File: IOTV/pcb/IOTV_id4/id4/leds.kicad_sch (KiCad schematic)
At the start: 50 parts, among them Q1 S8050, Q10 S8050, Q11 S8050, Q12 S8050, Q2 S8050, Q3 S8050, Q7 S8050, Q8 S8050, Q9 S8050

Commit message: PCB - ID4
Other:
- note added: "LED 5"
- note removed: "LED 0"

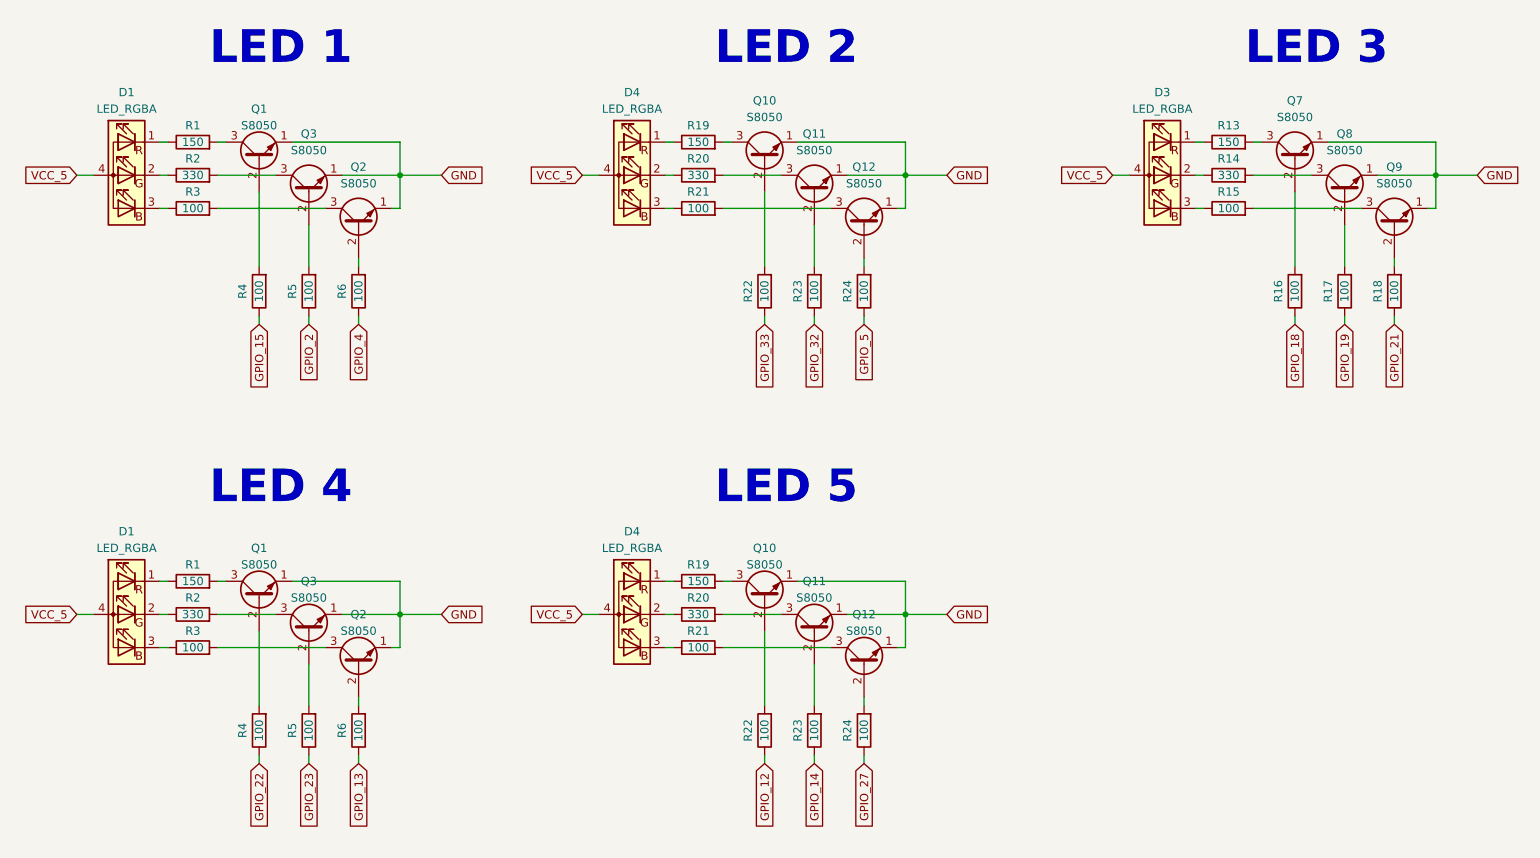
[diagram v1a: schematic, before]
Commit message: pcb id4 - rezonit OK
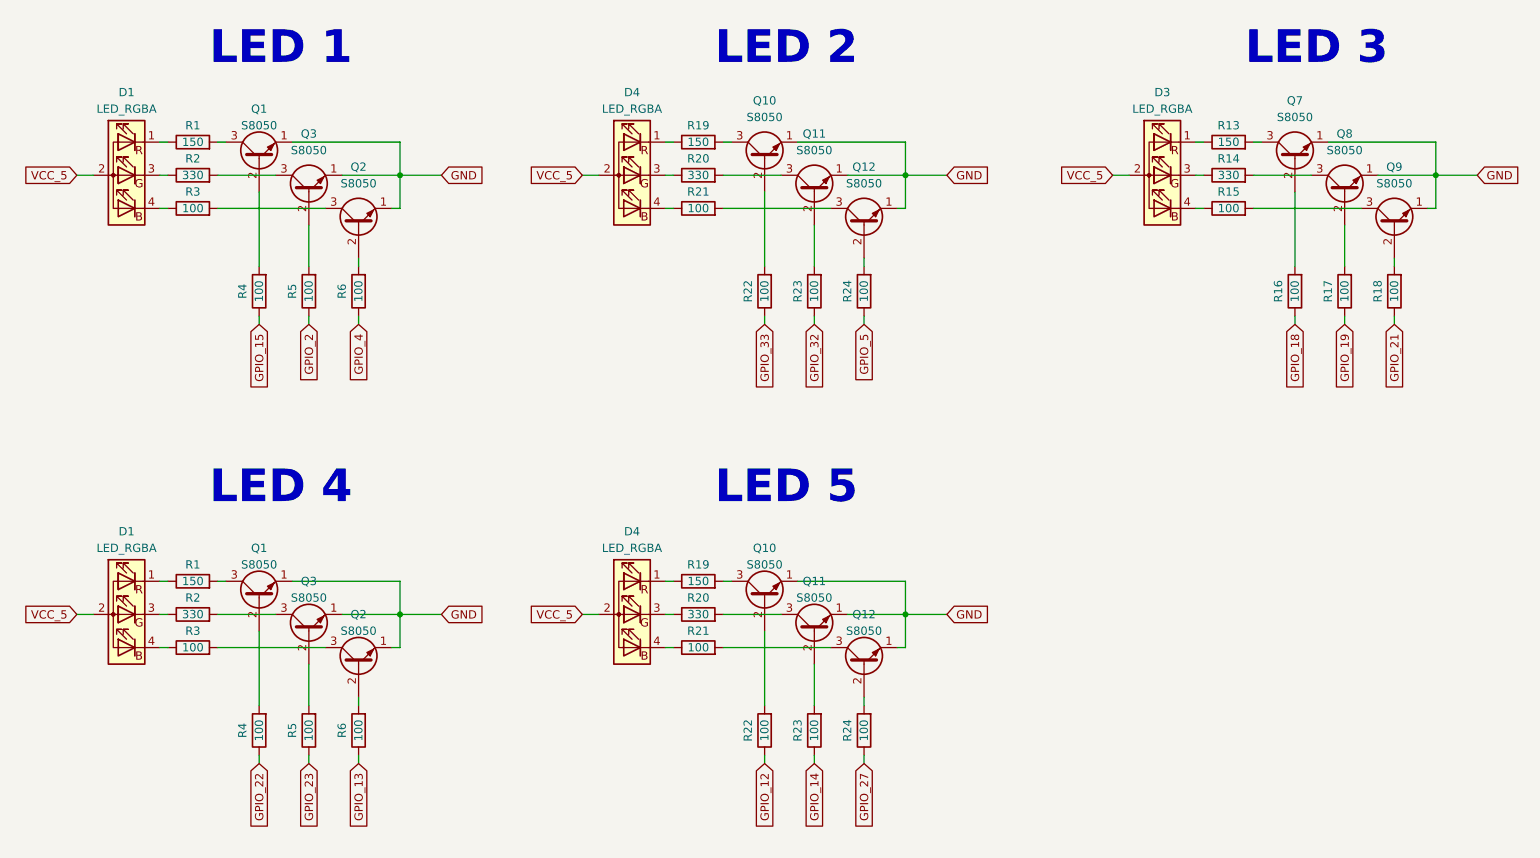
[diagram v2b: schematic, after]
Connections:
- net VCC_5: now also D1.2 (A), D1.2 (A), D3.2 (A), D4.2 (A), D4.2 (A); no longer D1.4 (A), D1.4 (A), D3.4 (A), D4.4 (A), D4.4 (A)
- net at R21.1: now also D4.4 (BK); no longer D4.3 (BK) (x2)
- net at R2.1: now also D1.3 (GK); no longer D1.2 (GK) (x2)
- net at R3.1: now also D1.4 (BK); no longer D1.3 (BK) (x2)
- net at R15.1: now also D3.4 (BK); no longer D3.3 (BK)
- net at R20.1: now also D4.3 (GK); no longer D4.2 (GK) (x2)
- net at R14.1: now also D3.3 (GK); no longer D3.2 (GK)
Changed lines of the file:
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@@
     )
   )
-  (symbol (lib_id "Device:LED_RGBA") (at 48.26 128.27 0) (mirror y) (unit 1)
+  (symbol (lib_name "LED_RGBA_4") (lib_id "Device:LED_RGBA") (at 48.26 128.27 0) (mirror y) (unit 1)
     (in_bom yes) (on_board yes) (dnp no)
     (property "Reference" "D1" (at 48.26 115.57 0)
@@
     )
     (pin "1")
-    (pin "2")
     (pin "3")
     (pin "4")
+    (pin "2")
     (instances
       (project "id4"
@@
     )
   )
-  (symbol (lib_id "Device:LED_RGBA") (at 125.73 60.96 0) (mirror y) (unit 1)
+  (symbol (lib_name "LED_RGBA_2") (lib_id "Device:LED_RGBA") (at 125.73 60.96 0) (mirror y) (unit 1)
     (in_bom yes) (on_board yes) (dnp no)
     (property "Reference" "D4" (at 125.73 48.26 0)
@@
     )
   )
-  (symbol (lib_id "Device:LED_RGBA") (at 48.26 60.96 0) (mirror y) (unit 1)
+  (symbol (lib_name "LED_RGBA_1") (lib_id "Device:LED_RGBA") (at 48.26 60.96 0) (mirror y) (unit 1)
     (in_bom yes) (on_board yes) (dnp no)
     (property "Reference" "D1" (at 48.26 48.26 0)
@@
     )
   )
-  (symbol (lib_id "Device:LED_RGBA") (at 207.01 60.96 0) (mirror y) (unit 1)
+  (symbol (lib_name "LED_RGBA_3") (lib_id "Device:LED_RGBA") (at 207.01 60.96 0) (mirror y) (unit 1)
     (in_bom yes) (on_board yes) (dnp no)
     (property "Reference" "D3" (at 207.01 48.26 0)

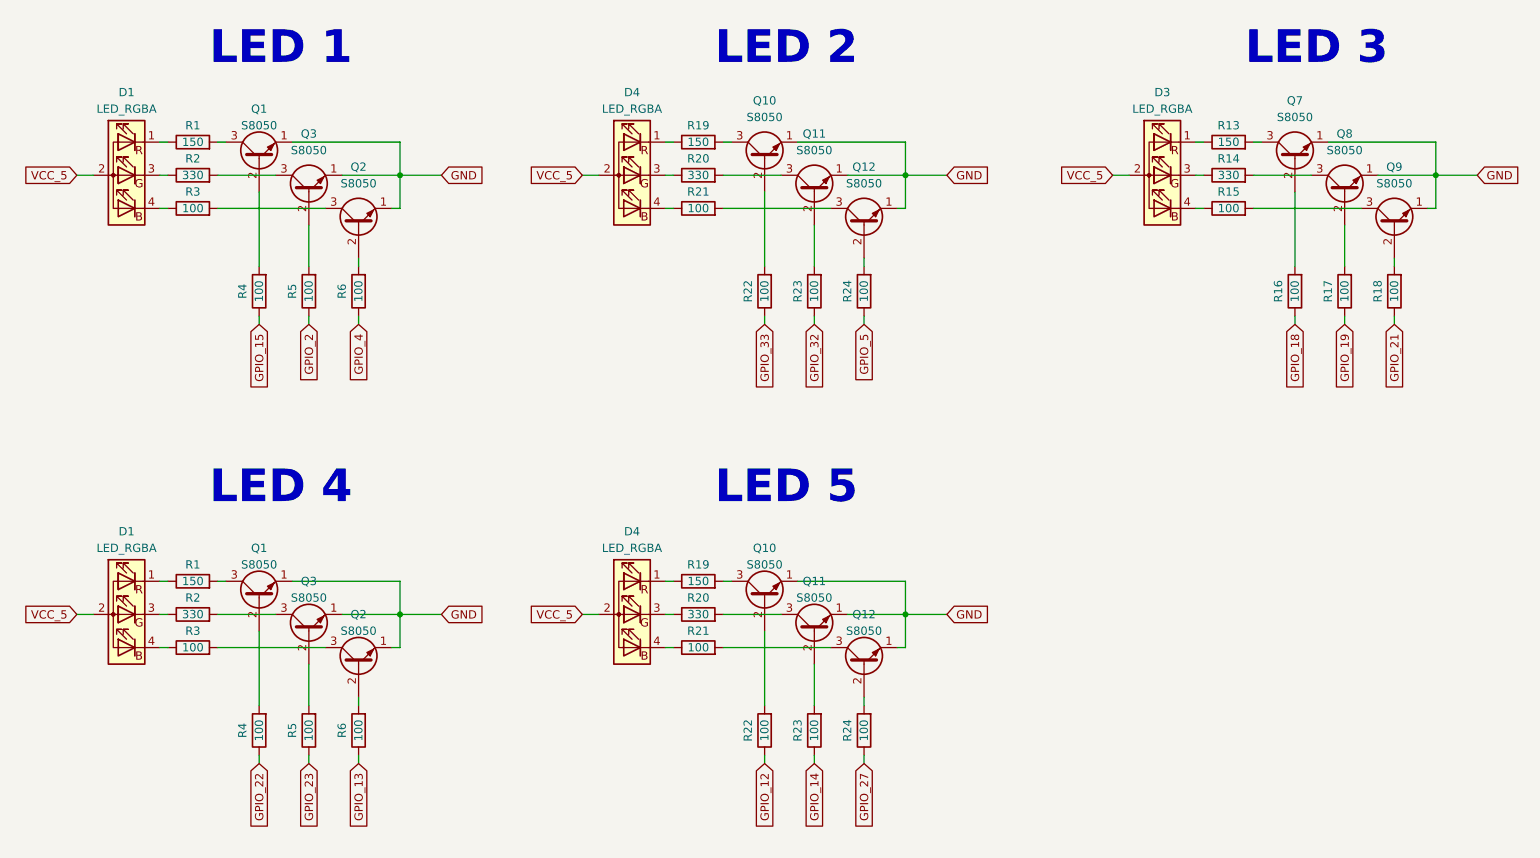
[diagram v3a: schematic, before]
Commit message: PCB id4 кнопки на землю
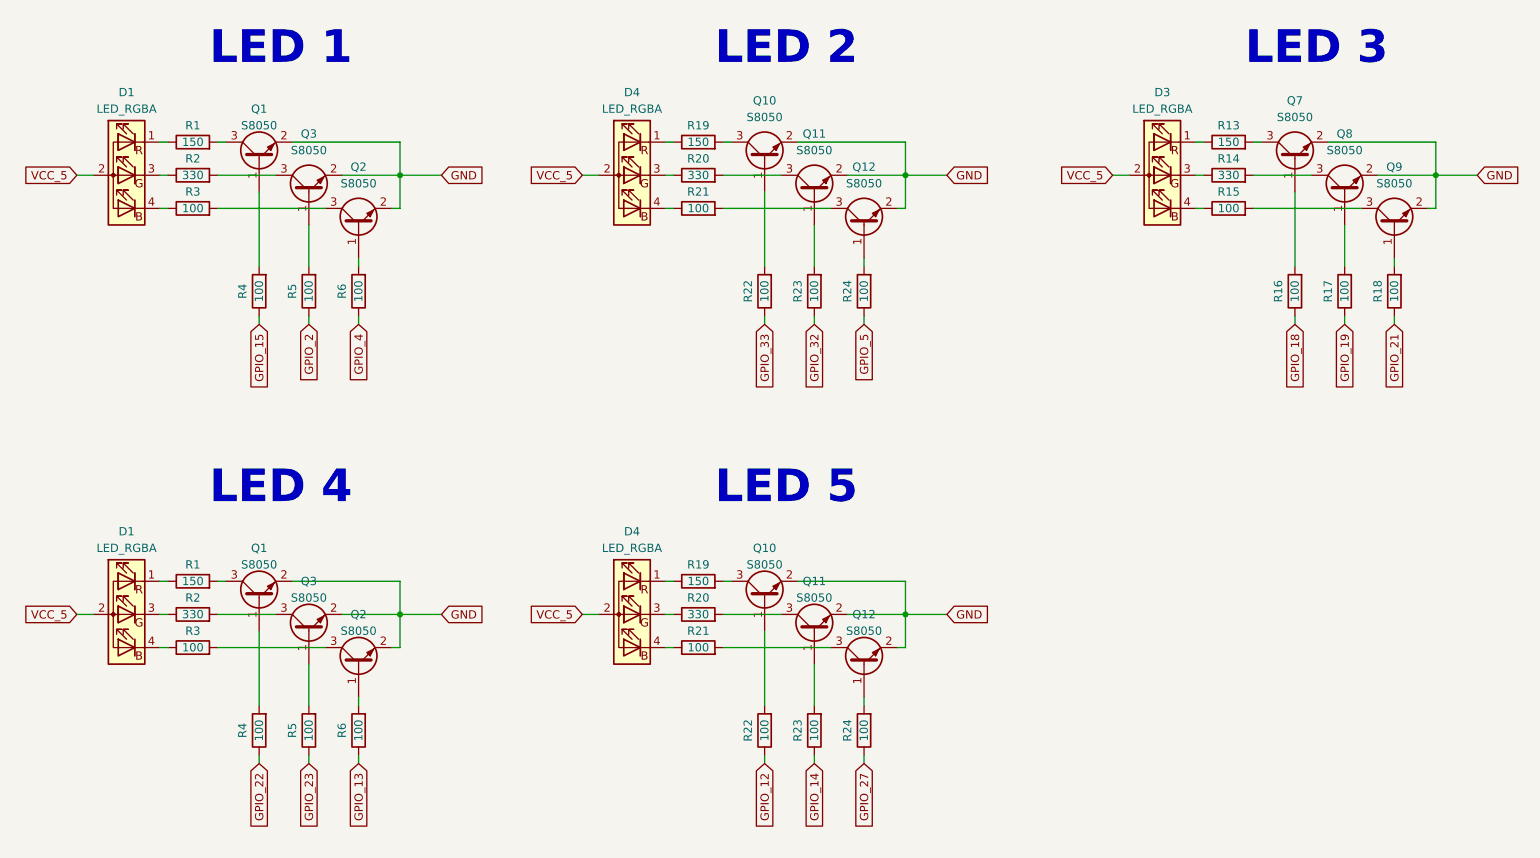
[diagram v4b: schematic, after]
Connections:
- net GND: now also Q1.2 (E), Q1.2 (E), Q10.2 (E), Q10.2 (E), Q11.2 (E), Q11.2 (E), Q12.2 (E), Q12.2 (E), Q2.2 (E), Q2.2 (E), Q3.2 (E), Q3.2 (E), Q7.2 (E), Q8.2 (E), Q9.2 (E); no longer Q1.1 (E), Q1.1 (E), Q10.1 (E), Q10.1 (E), Q11.1 (E), Q11.1 (E), Q12.1 (E), Q12.1 (E), Q2.1 (E), Q2.1 (E), Q3.1 (E), Q3.1 (E), Q7.1 (E), Q8.1 (E), Q9.1 (E)
- net at R16.2: now also Q7.1 (B); no longer Q7.2 (B)
- net at R24.2: now also Q12.1 (B); no longer Q12.2 (B) (x2)
- net at R6.2: now also Q2.1 (B); no longer Q2.2 (B) (x2)
- net at R5.2: now also Q3.1 (B); no longer Q3.2 (B) (x2)
- net at R4.2: now also Q1.1 (B); no longer Q1.2 (B) (x2)
- net at R22.2: now also Q10.1 (B); no longer Q10.2 (B) (x2)
- net at R23.2: now also Q11.1 (B); no longer Q11.2 (B) (x2)
- net at R17.2: now also Q8.1 (B); no longer Q8.2 (B)
- net at R18.2: now also Q9.1 (B); no longer Q9.2 (B)
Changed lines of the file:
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@@
     )
   )
-  (symbol (lib_id "Transistor_BJT:S8050") (at 227.33 58.42 90) (unit 1)
+  (symbol (lib_name "S8050_7") (lib_id "Transistor_BJT:S8050") (at 227.33 58.42 90) (unit 1)
     (in_bom yes) (on_board yes) (dnp no) (fields_autoplaced)
     (property "Reference" "Q7" (at 227.33 49.53 90)
@@
     )
   )
-  (symbol (lib_id "Transistor_BJT:S8050") (at 68.58 125.73 90) (unit 1)
+  (symbol (lib_name "S8050_10") (lib_id "Transistor_BJT:S8050") (at 68.58 125.73 90) (unit 1)
     (in_bom yes) (on_board yes) (dnp no) (fields_autoplaced)
     (property "Reference" "Q1" (at 68.58 118.11 90)
@@
     )
   )
-  (symbol (lib_id "Transistor_BJT:S8050") (at 76.2 130.81 90) (unit 1)
+  (symbol (lib_name "S8050_11") (lib_id "Transistor_BJT:S8050") (at 76.2 130.81 90) (unit 1)
     (in_bom yes) (on_board yes) (dnp no) (fields_autoplaced)
     (property "Reference" "Q3" (at 76.2 123.19 90)
@@
     )
   )
-  (symbol (lib_id "Transistor_BJT:S8050") (at 68.58 58.42 90) (unit 1)
+  (symbol (lib_name "S8050_1") (lib_id "Transistor_BJT:S8050") (at 68.58 58.42 90) (unit 1)
     (in_bom yes) (on_board yes) (dnp no) (fields_autoplaced)
     (property "Reference" "Q1" (at 68.58 50.8 90)
@@
     )
   )
-  (symbol (lib_id "Transistor_BJT:S8050") (at 146.05 58.42 90) (unit 1)
+  (symbol (lib_name "S8050_4") (lib_id "Transistor_BJT:S8050") (at 146.05 58.42 90) (unit 1)
     (in_bom yes) (on_board yes) (dnp no) (fields_autoplaced)
     (property "Reference" "Q10" (at 146.05 49.53 90)
@@
     )
   )
-  (symbol (lib_id "Transistor_BJT:S8050") (at 83.82 68.58 90) (unit 1)
+  (symbol (lib_name "S8050_3") (lib_id "Transistor_BJT:S8050") (at 83.82 68.58 90) (unit 1)
     (in_bom yes) (on_board yes) (dnp no) (fields_autoplaced)
     (property "Reference" "Q2" (at 83.82 59.69 90)
@@
     )
   )
-  (symbol (lib_id "Transistor_BJT:S8050") (at 146.05 125.73 90) (unit 1)
+  (symbol (lib_name "S8050_13") (lib_id "Transistor_BJT:S8050") (at 146.05 125.73 90) (unit 1)
     (in_bom yes) (on_board yes) (dnp no) (fields_autoplaced)
     (property "Reference" "Q10" (at 146.05 118.11 90)
@@
     )
   )
-  (symbol (lib_id "Transistor_BJT:S8050") (at 153.67 130.81 90) (unit 1)
+  (symbol (lib_name "S8050_14") (lib_id "Transistor_BJT:S8050") (at 153.67 130.81 90) (unit 1)
     (in_bom yes) (on_board yes) (dnp no) (fields_autoplaced)
     (property "Reference" "Q11" (at 153.67 123.19 90)
@@
     )
   )
-  (symbol (lib_id "Transistor_BJT:S8050") (at 76.2 63.5 90) (unit 1)
+  (symbol (lib_name "S8050_2") (lib_id "Transistor_BJT:S8050") (at 76.2 63.5 90) (unit 1)
     (in_bom yes) (on_board yes) (dnp no) (fields_autoplaced)
     (property "Reference" "Q3" (at 76.2 54.61 90)
@@
     )
   )
-  (symbol (lib_id "Transistor_BJT:S8050") (at 242.57 68.58 90) (unit 1)
+  (symbol (lib_name "S8050_9") (lib_id "Transistor_BJT:S8050") (at 242.57 68.58 90) (unit 1)
     (in_bom yes) (on_board yes) (dnp no) (fields_autoplaced)
     (property "Reference" "Q9" (at 242.57 59.69 90)
@@
     )
   )
-  (symbol (lib_id "Transistor_BJT:S8050") (at 161.29 68.58 90) (unit 1)
+  (symbol (lib_name "S8050_6") (lib_id "Transistor_BJT:S8050") (at 161.29 68.58 90) (unit 1)
     (in_bom yes) (on_board yes) (dnp no) (fields_autoplaced)
     (property "Reference" "Q12" (at 161.29 59.69 90)
@@
     )
   )
-  (symbol (lib_id "Transistor_BJT:S8050") (at 83.82 135.89 90) (unit 1)
+  (symbol (lib_name "S8050_12") (lib_id "Transistor_BJT:S8050") (at 83.82 135.89 90) (unit 1)
     (in_bom yes) (on_board yes) (dnp no) (fields_autoplaced)
     (property "Reference" "Q2" (at 83.82 128.27 90)
@@
     )
   )
-  (symbol (lib_id "Transistor_BJT:S8050") (at 153.67 63.5 90) (unit 1)
+  (symbol (lib_name "S8050_5") (lib_id "Transistor_BJT:S8050") (at 153.67 63.5 90) (unit 1)
     (in_bom yes) (on_board yes) (dnp no) (fields_autoplaced)
     (property "Reference" "Q11" (at 153.67 54.61 90)
@@
     )
   )
-  (symbol (lib_id "Transistor_BJT:S8050") (at 234.95 63.5 90) (unit 1)
+  (symbol (lib_name "S8050_8") (lib_id "Transistor_BJT:S8050") (at 234.95 63.5 90) (unit 1)
     (in_bom yes) (on_board yes) (dnp no) (fields_autoplaced)
     (property "Reference" "Q8" (at 234.95 54.61 90)
